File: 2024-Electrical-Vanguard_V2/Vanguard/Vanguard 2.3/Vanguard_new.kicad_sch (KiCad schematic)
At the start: 86 parts, among them J1 USB_C_Receptacle_USB2.0_16P, J2 Conn_02x03_Pin, J3 Micro_SD_Card_Det1, J4 STARBOARD_SERVO, J5 PORTSIDE_SERVO, J6 Battery In, J7 EJECTION_SERVO, Q1 BSS138, Q2 BSS138, Q3 BSS138, Q4 BSS138, U1 ATSAMD11D14A-M, U2 ATmega4809-A, U3 AT25DF641A-SH-T, U4 AP2112K-3.3, U5 BD1020HFV, U6 BNO086, U7 TXB0104D, U8 TPS61092, U9 MPM3610AGQV-P, Y1 32.768kHz

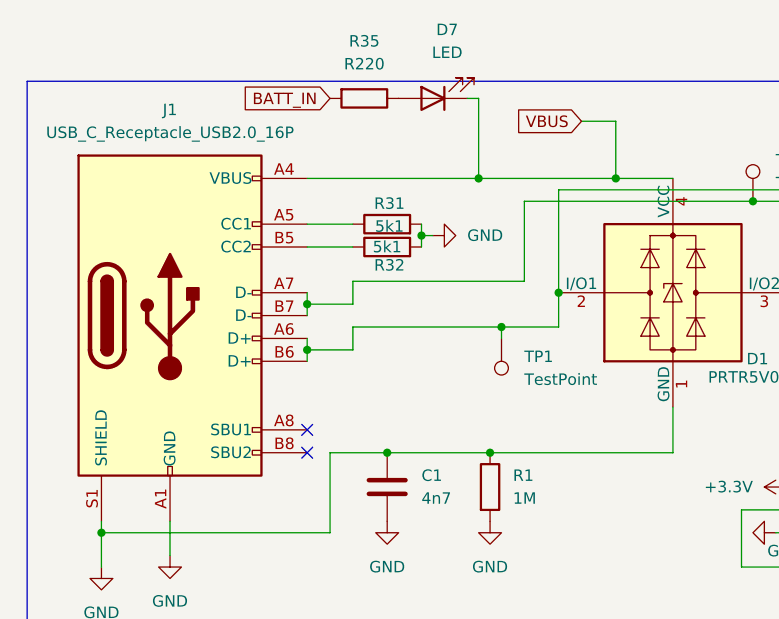
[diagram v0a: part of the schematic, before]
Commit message: fixed a small battery error
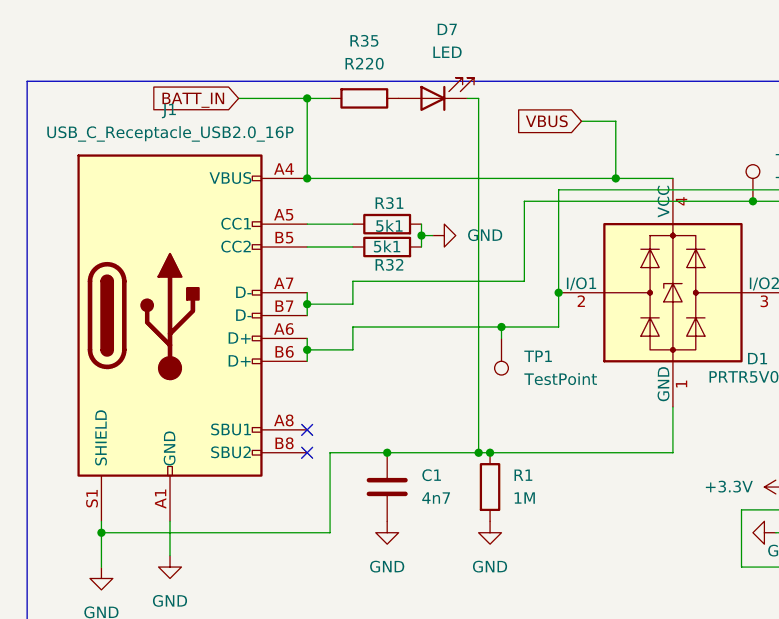
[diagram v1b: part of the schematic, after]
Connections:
- net BATT_IN: now also D1.4 (VCC), D6.2 (A), J1.A4 (VBUS), J1.A9 (VBUS), J1.B4 (VBUS), J1.B9 (VBUS)
- net GND: now also D7.1 (K)
- removed net VBUS: D1.4 (VCC), D6.2 (A), D7.1 (K), J1.A4 (VBUS), J1.A9 (VBUS), J1.B4 (VBUS), J1.B9 (VBUS)
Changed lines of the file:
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@@
+	)
+	(junction
+		(at 43.18 15.24)
+		(diameter 0)
+		(color 0 0 0 0)
 	)
 	(junction
@@
 	)
 	(junction
+		(at 62.23 54.61)
+		(diameter 0)
+		(color 0 0 0 0)
+	)
+	(junction
 		(at 311.15 119.38)
 		(diameter 0)
@@
 	)
 	(junction
+		(at 43.18 24.13)
+		(diameter 0)
+		(color 0 0 0 0)
+	)
+	(junction
 		(at 187.96 43.18)
 		(diameter 0)
@@
 	)
 	(junction
-		(at 62.23 24.13)
-		(diameter 0)
-		(color 0 0 0 0)
-	)
-	(junction
 		(at 377.19 114.3)
 		(diameter 0)
@@
 	(wire
 		(pts
-			(xy 52.07 54.61) (xy 63.5 54.61)
+			(xy 52.07 54.61) (xy 62.23 54.61)
 		)
 		(stroke
@@
 	(wire
 		(pts
+			(xy 62.23 15.24) (xy 62.23 54.61)
+		)
+		(stroke
+			(width 0)
+			(type default)
+		)
+	)
+	(wire
+		(pts
 			(xy 345.44 157.48) (xy 347.98 157.48)
 		)
@@
 	(wire
 		(pts
+			(xy 35.56 15.24) (xy 43.18 15.24)
+		)
+		(stroke
+			(width 0)
+			(type default)
+		)
+	)
+	(wire
+		(pts
 			(xy 59.69 238.76) (xy 53.34 238.76)
 		)
@@
 	(wire
 		(pts
+			(xy 43.18 15.24) (xy 43.18 24.13)
+		)
+		(stroke
+			(width 0)
+			(type default)
+		)
+	)
+	(wire
+		(pts
 			(xy 59.69 233.68) (xy 53.34 233.68)
 		)
@@
 	(wire
 		(pts
-			(xy 62.23 15.24) (xy 62.23 24.13)
-		)
-		(stroke
-			(width 0)
-			(type default)
-		)
-	)
-	(wire
-		(pts
 			(xy 57.15 132.08) (xy 62.23 132.08)
 		)
@@
 	(wire
 		(pts
-			(xy 43.18 24.13) (xy 62.23 24.13)
+			(xy 43.18 24.13) (xy 77.47 24.13)
 		)
 		(stroke
@@
 	(wire
 		(pts
+			(xy 62.23 54.61) (xy 63.5 54.61)
+		)
+		(stroke
+			(width 0)
+			(type default)
+		)
+	)
+	(wire
+		(pts
 			(xy 222.25 58.42) (xy 219.71 58.42)
 		)
@@
 	(wire
 		(pts
+			(xy 43.18 15.24) (xy 45.72 15.24)
+		)
+		(stroke
+			(width 0)
+			(type default)
+		)
+	)
+	(wire
+		(pts
 			(xy 157.48 231.14) (xy 158.75 231.14)
 		)
@@
 		(pts
 			(xy 72.39 240.03) (xy 59.69 240.03)
-		)
-		(stroke
-			(width 0)
-			(type default)
-		)
-	)
-	(wire
-		(pts
-			(xy 62.23 24.13) (xy 77.47 24.13)
 		)
 		(stroke
@@
 	(global_label "BATT_IN"
 		(shape input)
-		(at 45.72 15.24 180)
+		(at 35.56 15.24 180)
 		(fields_autoplaced yes)
 		(effects
@@
 		)
 		(property "Intersheetrefs" "${INTERSHEET_REFS}"
-			(at 35.5381 15.24 0)
+			(at 25.3781 15.24 0)
 			(effects
 				(font
